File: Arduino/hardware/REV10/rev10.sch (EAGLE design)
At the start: 41 parts, among them IC2 ATMEGA168-AU, Q1 32768Hz, Q2 BSS84, U1 TC1185SMD, U2 ARDUINOR3-DIMENSION

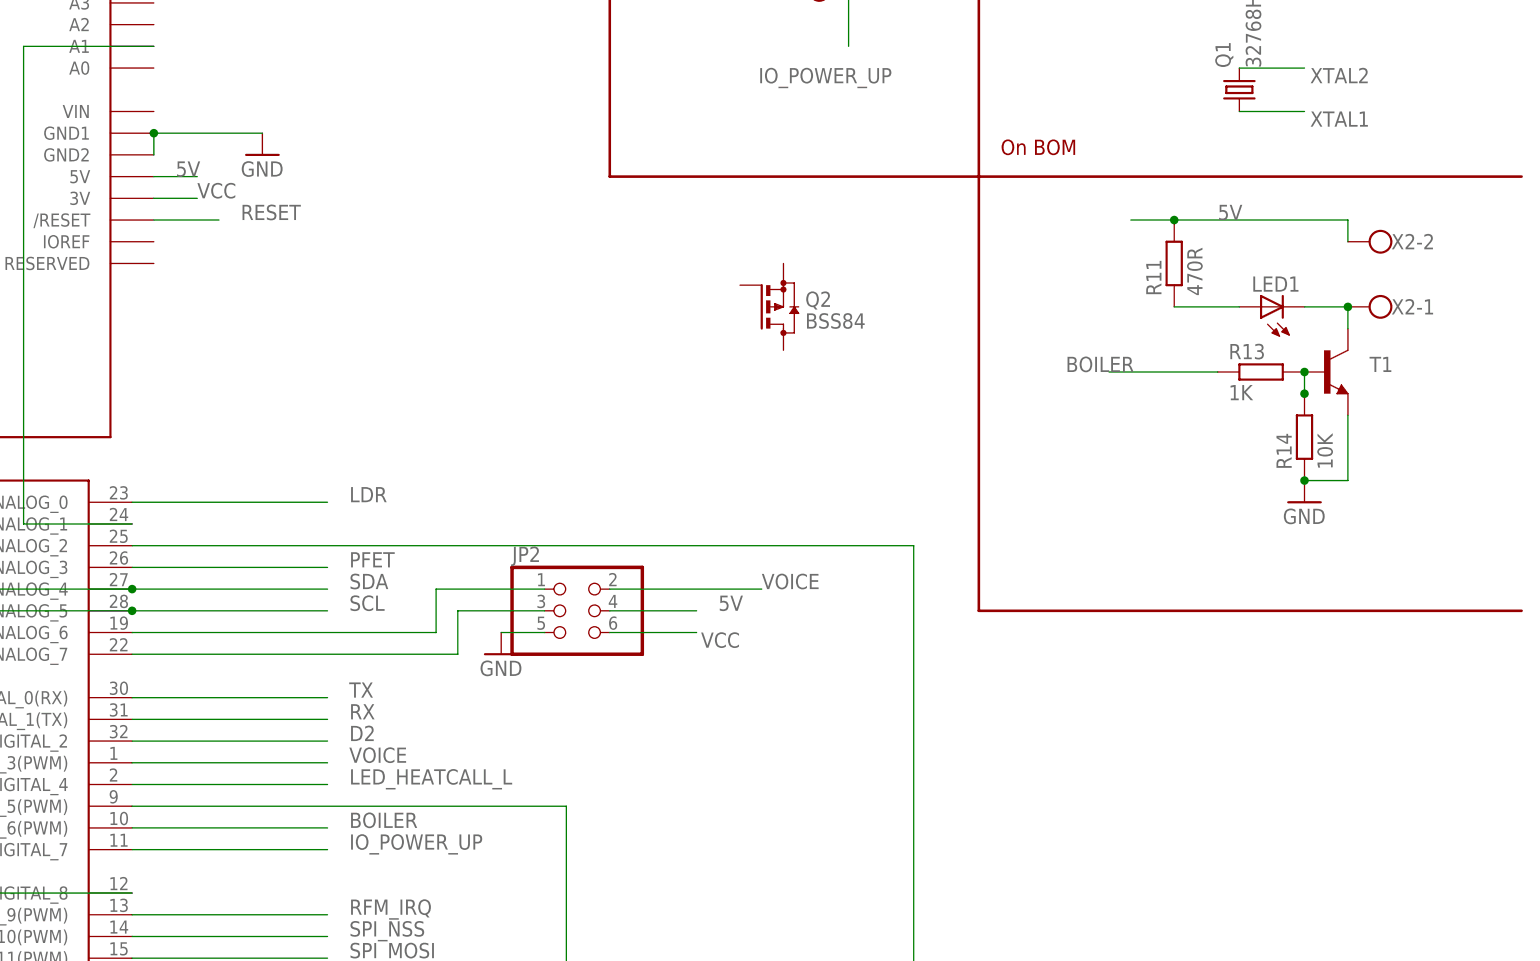
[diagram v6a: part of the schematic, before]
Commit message: added relay on board
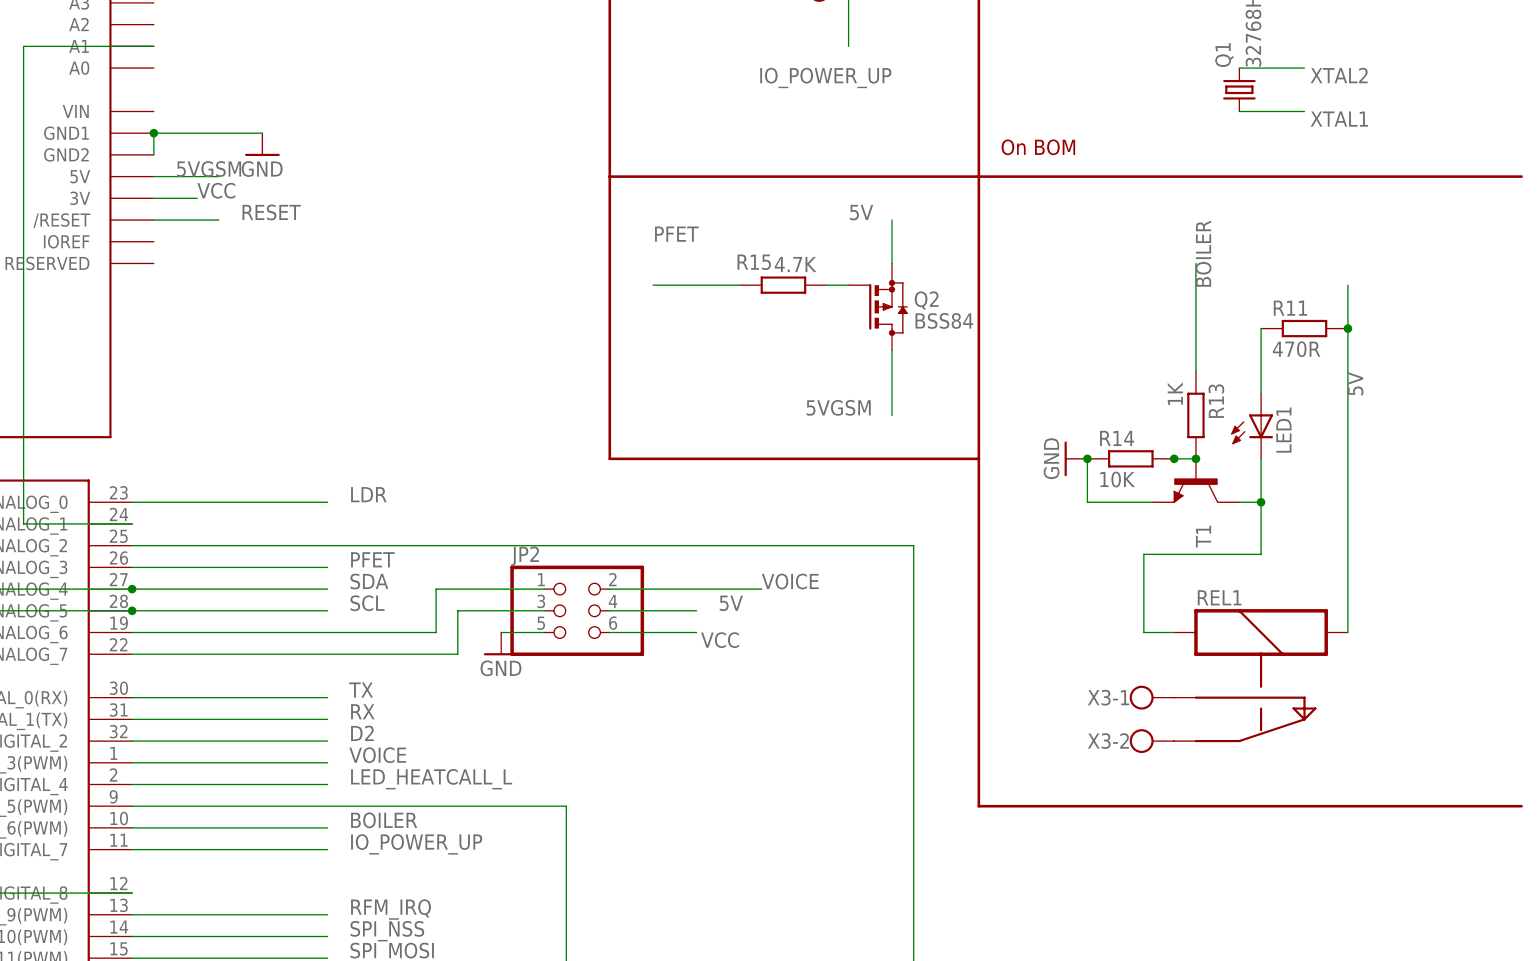
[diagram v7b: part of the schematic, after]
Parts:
- removed X2: (no value), con-wago-500:W237-102
- added R15: 4.7K, resistor:R-EU_R0603
- added REL1: (no value), ALDP105:ALDP105
- added X3: (no value), con-wago-500:W237-102
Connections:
- new net 5VGSM: Q2.D
- new net N$17: Q2.G, R15.1
- new net N$22: REL1.C, X3-2.KL
- new net N$24: REL1.S, X3-1.KL
- new net PFET: R15.2
- net 5V: now also Q2.S, REL1.S2; no longer X2-2.KL
- net N$14: now also REL1.S1; no longer X2-1.KL
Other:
- moved on the sheet: LED1, Q2, R11, R13, R14, T1
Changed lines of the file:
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@@
 <part name="R14" library="resistor" deviceset="R-EU_" device="R0603" value="10K"/>
 <part name="GND10" library="SparkFun-Aesthetics" deviceset="GND" device=""/>
-<part name="X2" library="con-wago-500" deviceset="W237-102" device=""/>
 <part name="JP2" library="pinhead" deviceset="PINHD-2X3" device="/90"/>
 <part name="Q2" library="transistor-small-signal" deviceset="BSS84" device=""/>
+<part name="R15" library="resistor" deviceset="R-EU_" device="R0603" value="4.7K"/>
+<part name="REL1" library="ALDP105" deviceset="ALDP105" device=""/>
+<part name="X3" library="con-wago-500" deviceset="W237-102" device=""/>
 </parts>
 <sheets>
@@
 <text x="45.72" y="175.26" size="1.778" layer="94" rot="R180">On BOM</text>
 <text x="137.16" y="210.82" size="1.778" layer="94" rot="R90">On BOM</text>
-<wire x1="325.12" y1="157.48" x2="325.12" y2="106.68" width="0.3048" layer="94"/>
-<wire x1="325.12" y1="106.68" x2="388.62" y2="106.68" width="0.3048" layer="94"/>
+<wire x1="325.12" y1="157.48" x2="325.12" y2="124.46" width="0.3048" layer="94"/>
+<wire x1="325.12" y1="124.46" x2="325.12" y2="83.82" width="0.3048" layer="94"/>
+<wire x1="325.12" y1="83.82" x2="388.62" y2="83.82" width="0.3048" layer="94"/>
+<wire x1="281.94" y1="157.48" x2="281.94" y2="124.46" width="0.3048" layer="94"/>
+<wire x1="281.94" y1="124.46" x2="325.12" y2="124.46" width="0.3048" layer="94"/>
 </plain>
 <instances>
@@
 <instance part="GND6" gate="1" x="269.24" y="101.6"/>
 <instance part="GND9" gate="1" x="157.48" y="139.7"/>
-<instance part="R11" gate="G$1" x="347.98" y="147.32" rot="R90"/>
-<instance part="LED1" gate="G$1" x="358.14" y="142.24" rot="R90"/>
-<instance part="T1" gate="G$1" x="365.76" y="134.62" smashed="yes">
-<attribute name="NAME" x="370.84" y="134.62" size="1.778" layer="95"/>
-<attribute name="VALUE" x="355.6" y="139.7" size="1.778" layer="96"/>
+<instance part="R11" gate="G$1" x="363.22" y="139.7"/>
+<instance part="LED1" gate="G$1" x="358.14" y="129.54"/>
+<instance part="T1" gate="G$1" x="350.52" y="121.92" smashed="yes" rot="R270">
+<attribute name="NAME" x="350.52" y="116.84" size="1.778" layer="95" rot="R270"/>
+<attribute name="VALUE" x="355.6" y="132.08" size="1.778" layer="96" rot="R270"/>
 </instance>
-<instance part="R13" gate="G$1" x="358.14" y="134.62"/>
-<instance part="R14" gate="G$1" x="363.22" y="127" rot="R90"/>
-<instance part="GND10" gate="1" x="363.22" y="119.38"/>
-<instance part="X2" gate="-1" x="373.38" y="142.24" rot="R180"/>
-<instance part="X2" gate="-2" x="373.38" y="149.86" rot="R180"/>
+<instance part="R13" gate="G$1" x="350.52" y="129.54" rot="R270"/>
+<instance part="R14" gate="G$1" x="342.9" y="124.46"/>
+<instance part="GND10" gate="1" x="335.28" y="124.46" rot="R270"/>
 <instance part="JP2" gate="A" x="276.86" y="106.68"/>
-<instance part="Q2" gate="G$1" x="302.26" y="142.24"/>
+<instance part="Q2" gate="G$1" x="314.96" y="142.24"/>
+<instance part="R15" gate="G$1" x="302.26" y="144.78" smashed="yes" rot="R180">
+<attribute name="NAME" x="300.99" y="148.3614" size="1.778" layer="95" rot="R180"/>
+<attribute name="VALUE" x="306.07" y="148.082" size="1.778" layer="96" rot="R180"/>
+</instance>
+<instance part="REL1" gate="G$1" x="358.14" y="93.98" rot="R270"/>
+<instance part="X3" gate="-1" x="342.9" y="96.52"/>
+<instance part="X3" gate="-2" x="342.9" y="91.44"/>
 </instances>
 <busses>
@@
 <pinref part="GND10" gate="1" pin="GND"/>
 <pinref part="T1" gate="G$1" pin="E"/>
-<wire x1="363.22" y1="121.92" x2="368.3" y2="121.92" width="0.1524" layer="91"/>
-<wire x1="368.3" y1="121.92" x2="368.3" y2="129.54" width="0.1524" layer="91"/>
-<junction x="363.22" y="121.92"/>
+<wire x1="337.82" y1="124.46" x2="337.82" y2="119.38" width="0.1524" layer="91"/>
+<wire x1="337.82" y1="119.38" x2="345.44" y2="119.38" width="0.1524" layer="91"/>
+<junction x="337.82" y="124.46"/>
 </segment>
 </net>
@@
 <segment>
 <pinref part="R13" gate="G$1" pin="1"/>
-<wire x1="353.06" y1="134.62" x2="340.36" y2="134.62" width="0.1524" layer="91"/>
-<label x="335.28" y="134.62" size="1.778" layer="95"/>
+<wire x1="350.52" y1="134.62" x2="350.52" y2="147.32" width="0.1524" layer="91"/>
+<label x="350.52" y="152.4" size="1.778" layer="95" rot="R270"/>
 </segment>
 </net>
@@
 </segment>
 <segment>
-<wire x1="233.68" y1="157.48" x2="228.6" y2="157.48" width="0.1524" layer="91"/>
-<label x="231.14" y="157.48" size="1.778" layer="95"/>
-</segment>
-<segment>
 <wire x1="292.1" y1="106.68" x2="281.94" y2="106.68" width="0.1524" layer="91"/>
 <label x="294.64" y="106.68" size="1.778" layer="95"/>
@@
 </segment>
 <segment>
-<wire x1="342.9" y1="152.4" x2="347.98" y2="152.4" width="0.1524" layer="91"/>
-<label x="353.06" y="152.4" size="1.778" layer="95"/>
+<wire x1="368.3" y1="144.78" x2="368.3" y2="139.7" width="0.1524" layer="91"/>
+<label x="368.3" y="134.62" size="1.778" layer="95" rot="R270"/>
 <pinref part="R11" gate="G$1" pin="2"/>
-<junction x="347.98" y="152.4"/>
-<pinref part="X2" gate="-2" pin="KL"/>
-<wire x1="347.98" y1="152.4" x2="368.3" y2="152.4" width="0.1524" layer="91"/>
-<wire x1="368.3" y1="152.4" x2="368.3" y2="149.86" width="0.1524" layer="91"/>
+<junction x="368.3" y="139.7"/>
+<wire x1="368.3" y1="139.7" x2="368.3" y2="104.14" width="0.1524" layer="91"/>
+<pinref part="REL1" gate="G$1" pin="S2"/>
+</segment>
+<segment>
+<wire x1="314.96" y1="147.32" x2="314.96" y2="152.4" width="0.1524" layer="91"/>
+<label x="309.88" y="152.4" size="1.778" layer="95"/>
+<pinref part="Q2" gate="G$1" pin="S"/>
 </segment>
 </net>
@@
 <label x="251.46" y="111.76" size="1.778" layer="95"/>
 </segment>
+<segment>
+<wire x1="297.18" y1="144.78" x2="287.02" y2="144.78" width="0.1524" layer="91"/>
+<label x="287.02" y="149.86" size="1.778" layer="95"/>
+<pinref part="R15" gate="G$1" pin="2"/>
+</segment>
 </net>
 <net name="N$20" class="0">
@@
 <pinref part="R13" gate="G$1" pin="2"/>
 <pinref part="R14" gate="G$1" pin="2"/>
-<junction x="363.22" y="132.08"/>
+<junction x="347.98" y="124.46"/>
 <pinref part="R14" gate="G$1" pin="2"/>
-<wire x1="363.22" y1="132.08" x2="363.22" y2="134.62" width="0.1524" layer="91"/>
-<junction x="363.22" y="134.62"/>
+<wire x1="347.98" y1="124.46" x2="350.52" y2="124.46" width="0.1524" layer="91"/>
+<junction x="350.52" y="124.46"/>
 </segment>
 </net>
@@
 <segment>
 <pinref part="T1" gate="G$1" pin="C"/>
-<wire x1="363.22" y1="142.24" x2="368.3" y2="142.24" width="0.1524" layer="91"/>
-<wire x1="368.3" y1="142.24" x2="368.3" y2="139.7" width="0.1524" layer="91"/>
+<wire x1="358.14" y1="124.46" x2="358.14" y2="119.38" width="0.1524" layer="91"/>
+<wire x1="358.14" y1="119.38" x2="355.6" y2="119.38" width="0.1524" layer="91"/>
 <pinref part="LED1" gate="G$1" pin="C"/>
-<pinref part="X2" gate="-1" pin="KL"/>
-<junction x="368.3" y="142.24"/>
+<wire x1="358.14" y1="119.38" x2="358.14" y2="113.284" width="0.1524" layer="91"/>
+<wire x1="358.14" y1="113.284" x2="344.424" y2="113.284" width="0.1524" layer="91"/>
+<junction x="358.14" y="119.38"/>
+<pinref part="REL1" gate="G$1" pin="S1"/>
+<wire x1="344.424" y1="113.284" x2="344.424" y2="104.14" width="0.1524" layer="91"/>
+<wire x1="344.424" y1="104.14" x2="347.98" y2="104.14" width="0.1524" layer="91"/>
 </segment>
 </net>
@@
 <segment>
 <pinref part="R11" gate="G$1" pin="1"/>
-<wire x1="355.6" y1="142.24" x2="347.98" y2="142.24" width="0.1524" layer="91"/>
+<wire x1="358.14" y1="132.08" x2="358.14" y2="139.7" width="0.1524" layer="91"/>
 <pinref part="LED1" gate="G$1" pin="A"/>
 </segment>
 </net>
+<net name="N$17" class="0">
+<segment>
+<pinref part="R15" gate="G$1" pin="1"/>
+<pinref part="Q2" gate="G$1" pin="G"/>
+<wire x1="307.34" y1="144.78" x2="309.88" y2="144.78" width="0.1524" layer="91"/>
+</segment>
+</net>
+<net name="5VGSM" class="0">
+<segment>
+<pinref part="Q2" gate="G$1" pin="D"/>
+<wire x1="314.96" y1="137.16" x2="314.96" y2="129.54" width="0.1524" layer="91"/>
+<label x="304.8" y="129.54" size="1.778" layer="95"/>
+</segment>
+<segment>
+<wire x1="228.6" y1="157.48" x2="236.22" y2="157.48" width="0.1524" layer="91"/>
+<label x="231.14" y="157.48" size="1.778" layer="95"/>
+</segment>
+</net>
+<net name="N$22" class="0">
+<segment>
+<pinref part="REL1" gate="G$1" pin="C"/>
+<pinref part="X3" gate="-2" pin="KL"/>
+</segment>
+</net>
+<net name="N$24" class="0">
+<segment>
+<pinref part="REL1" gate="G$1" pin="S"/>
+<pinref part="X3" gate="-1" pin="KL"/>
+</segment>
+</net>

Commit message: before routing update
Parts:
- REL1: device ALDP105:ALDP105 -> OJE-SS-103HM:OJE-SS-103HM
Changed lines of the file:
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@@
 <part name="Q2" library="transistor-small-signal" deviceset="BSS84" device=""/>
 <part name="R15" library="resistor" deviceset="R-EU_" device="R0603" value="4.7K"/>
-<part name="REL1" library="ALDP105" deviceset="ALDP105" device=""/>
+<part name="REL1" library="OJE-SS-103HM" deviceset="OJE-SS-103HM" device=""/>
 <part name="X3" library="con-wago-500" deviceset="W237-102" device=""/>
 </parts>
